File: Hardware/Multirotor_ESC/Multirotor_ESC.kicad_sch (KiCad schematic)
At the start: 1 part

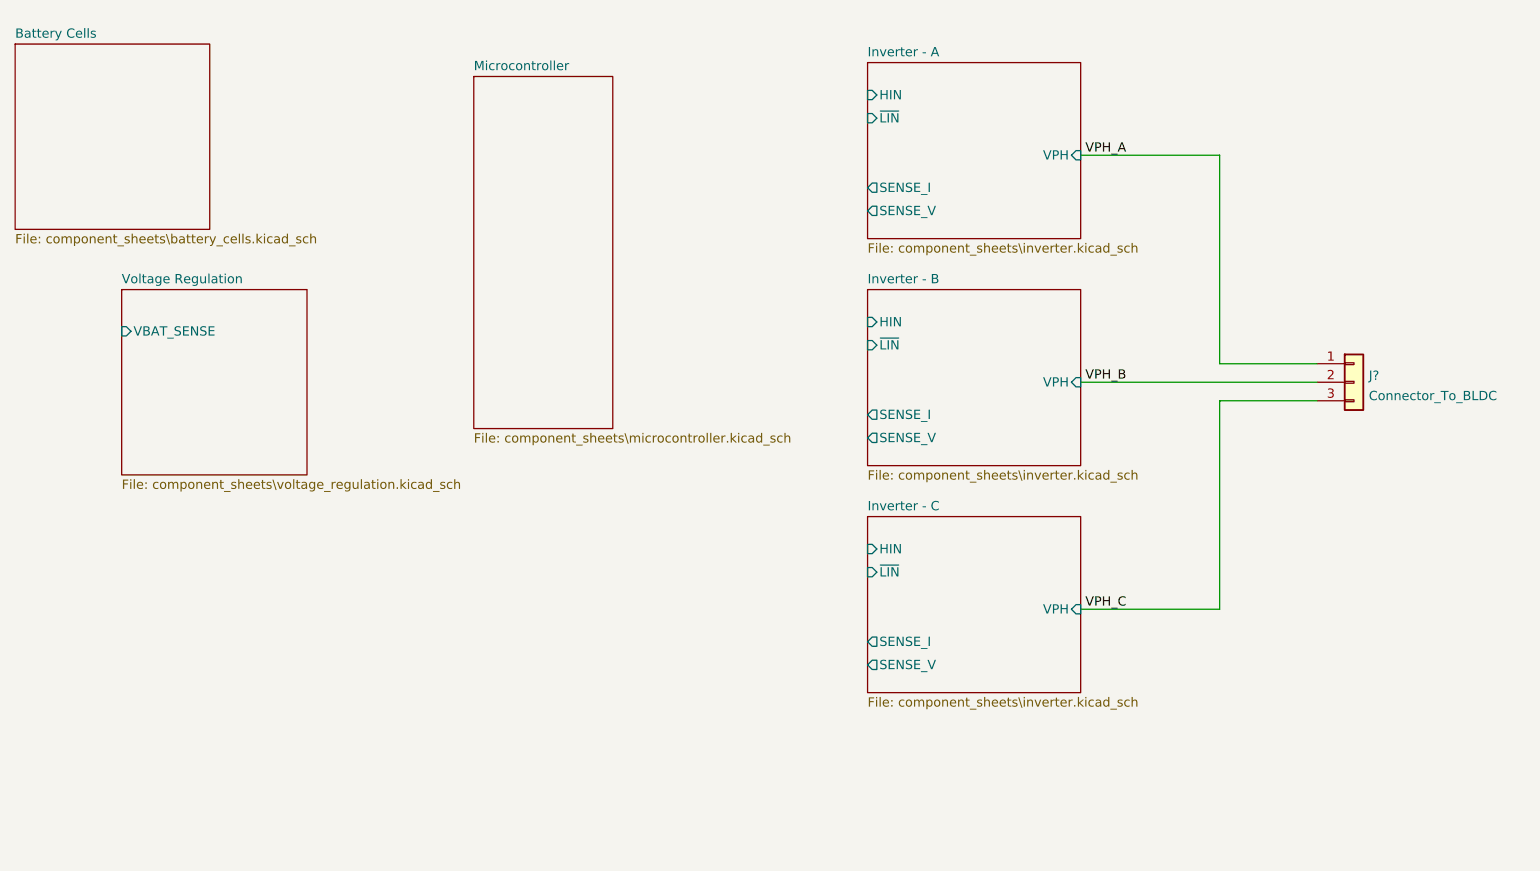
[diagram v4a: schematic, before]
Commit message: Improved component sheet labels
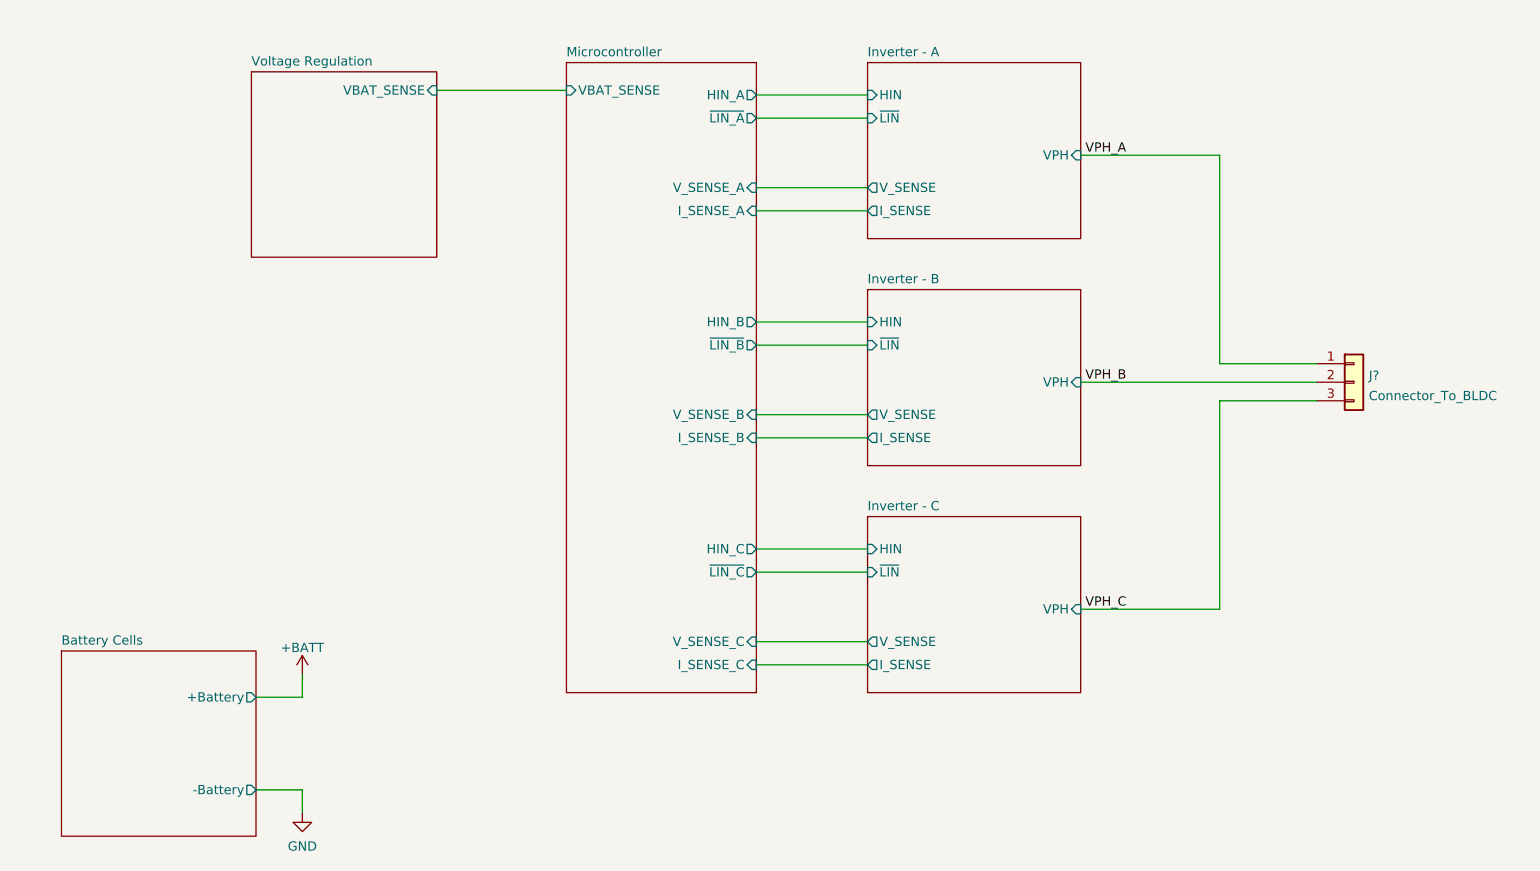
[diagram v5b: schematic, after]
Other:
- sheet Battery Cells ports: added +Battery, -Battery; removed none
- sheet Inverter - A ports: added I_SENSE, V_SENSE; removed SENSE_I, SENSE_V
- sheet Inverter - B ports: added I_SENSE, V_SENSE; removed SENSE_I, SENSE_V
- sheet Inverter - C ports: added I_SENSE, V_SENSE; removed SENSE_I, SENSE_V
- sheet Microcontroller ports: added HIN_A, HIN_B, HIN_C, I_SENSE_A, I_SENSE_B, I_SENSE_C, VBAT_SENSE, V_SENSE_A, V_SENSE_B, V_SENSE_C, ~{LIN_A}, ~{LIN_B}, ~{LIN_C}; removed none
